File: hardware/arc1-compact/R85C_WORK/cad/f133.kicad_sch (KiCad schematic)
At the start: 34 parts, among them U15 F133-B, Y1 24MHz

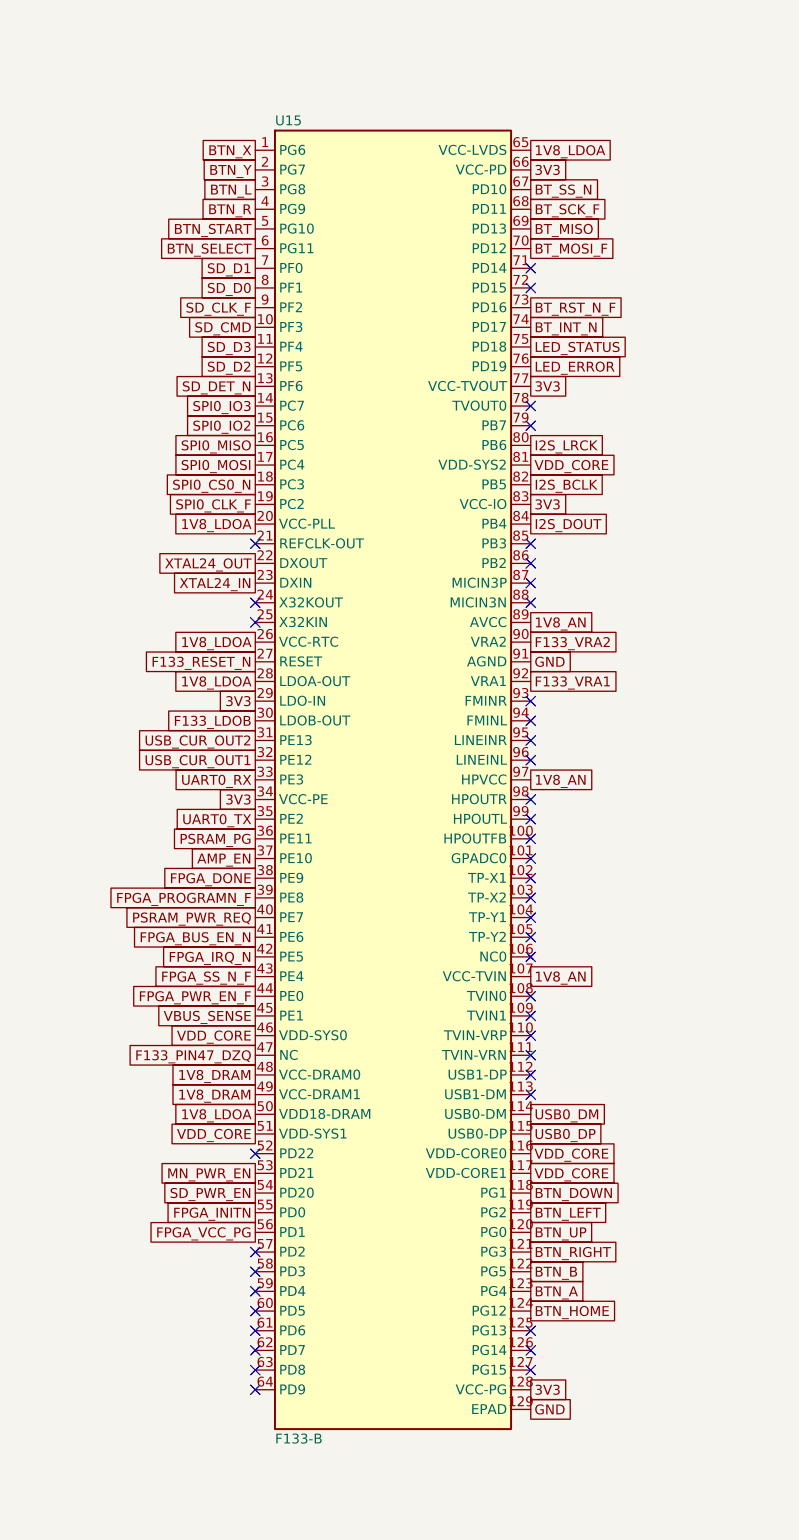
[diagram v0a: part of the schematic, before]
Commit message: R85C C3: RGMII on F133 PG0-PG12 to ECP5 bank 0, buttons moved to PD2-9/PD14/PD15/PD22/PB2/PB3
- design.py: 12 RGMII nets with 22R series resistors at each driver, 100k CTL pull-downs; RXCK onto PCLKT0_0 (B11)
- F133 mux transcription extended from DS rev 2.3 Table 4-3 (PG0-PG12, PD2-PD9, PD14, PD15)
- pin matrix / LPF generated from the board plan (identical to the C2 provisional LPF, which is removed);
  bitstream unchanged (087cb5a2...12be)
- board rule rgmii_link + 7 negative tests (17/17 rules, 37 tests pass); KiCad ERC 0/0; crosscheck PASS
- RGMII timing budget from F133 DS Table 5-21 and ECP5 DS-02012 Table 3.22: 0.53 / 0.53 / 0.5 ns, CONDITIONAL
  (board skew and delay-chain centring are assumptions); docs/RGMII_LINK_R85C.md
- firmware host tests 799/0 and freestanding build pass with the new pin header

Co-Authored-By: Claude Opus 5.5 <noreply@anthropic.com>
Claude-Session: https://claude.ai/code/session_01UkiuLdbjDvK75uDzAPKsGs
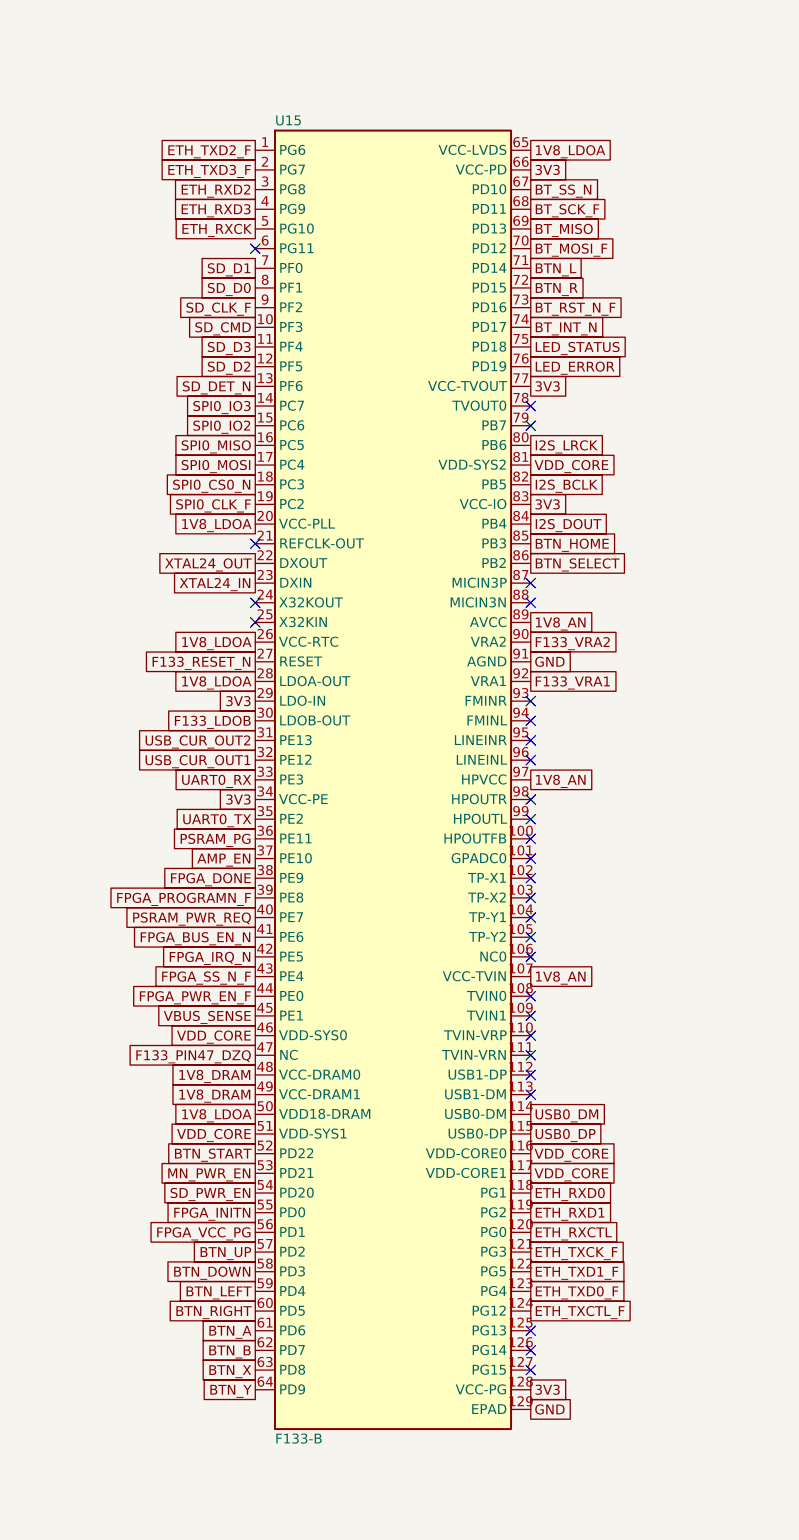
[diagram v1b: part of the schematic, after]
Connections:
- net BTN_A: now also U15.61 (PD6); no longer U15.123 (PG4)
- net BTN_B: now also U15.62 (PD7); no longer U15.122 (PG5)
- net BTN_DOWN: now also U15.58 (PD3); no longer U15.118 (PG1)
- net BTN_HOME: now also U15.85 (PB3); no longer U15.124 (PG12)
- net BTN_L: now also U15.71 (PD14); no longer U15.3 (PG8)
- net BTN_LEFT: now also U15.59 (PD4); no longer U15.119 (PG2)
- net BTN_R: now also U15.72 (PD15); no longer U15.4 (PG9)
- net BTN_RIGHT: now also U15.60 (PD5); no longer U15.121 (PG3)
- net BTN_SELECT: now also U15.86 (PB2); no longer U15.6 (PG11)
- net BTN_START: now also U15.52 (PD22); no longer U15.5 (PG10)
- net BTN_UP: now also U15.57 (PD2); no longer U15.120 (PG0)
- net BTN_X: now also U15.63 (PD8); no longer U15.1 (PG6)
- net BTN_Y: now also U15.64 (PD9); no longer U15.2 (PG7)
- new net ETH_RXCK: U15.5 (PG10)
- new net ETH_RXCTL: U15.120 (PG0)
- new net ETH_RXD0: U15.118 (PG1)
- new net ETH_RXD1: U15.119 (PG2)
- new net ETH_RXD2: U15.3 (PG8)
- new net ETH_RXD3: U15.4 (PG9)
- new net ETH_TXCK_F: U15.121 (PG3)
- new net ETH_TXCTL_F: U15.124 (PG12)
- new net ETH_TXD0_F: U15.123 (PG4)
- new net ETH_TXD1_F: U15.122 (PG5)
- new net ETH_TXD2_F: U15.1 (PG6)
- new net ETH_TXD3_F: U15.2 (PG7)
- no-connect marks 42 -> 30
